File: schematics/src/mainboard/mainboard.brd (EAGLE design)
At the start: 160 x 100 mm, 25 parts, among them IC1 MCP4921P, IC3 TL082P, IC4 TINY24/44/84-PU, Q1 16Mhz, T1 3904

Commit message: Updated Schematics & Firmware
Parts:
- added C12, C5, C6: 10uf, resistor:E2,5-5
- added C13, C14, C16, C17, C18: .1uF, rcl:C050-024X044
- added C15: 47pF, rcl:C050-024X044
- added CV_OFFSET: 20k, pot:S64YW
- added D1, D2: 1N4148, diode:DO35-7
- added D3, D4, D5, D6: 1n4148, diode:DO35-7
- added IC2, IC5, IC7: TL084P, linear:DIL14
- added IC6: 4013N, 40xx:DIL14
- added IO_CON1, IO_CON2: (no value), pinhead:1X04
- added JP1: (no value), pinhead:2X03
- added PWR: (no value), con-ml:ML10
- added PWR_CON: (no value), pinhead:1X03
- added R12, R25: 47k, rcl:0207/7
- added R13: 33k, rcl:0207/7
- added R14: 27k, rcl:0207/7
- added R15, R16, R17, R21, R30, R34: 100k .1%, rcl:0207/7
- added R18, R31: 200k .1%, rcl:0207/7
- added R19, R26: 6.8k, rcl:0207/7
- added R20: 68k, rcl:0207/7
- added R22, R24: 300k, rcl:0207/7
- added R23, R32, R42: 150k, rcl:0207/7
- added R27: 20k 1%, rcl:0207/7
- added R28: 24k 1%, rcl:0207/7
- added R29: 18k, rcl:0207/7
- added R33: 50k .1%, rcl:0207/7
- added R35, R38: 10k, rcl:0207/7
- added R36: 470k, rcl:0207/7
- added R37: 12k, rcl:0207/7
- added R39: 22k, rcl:0207/7
- added R40: 15k, rcl:0207/7
- added R41: 1.2k, rcl:0207/7
- added TP1, TP2: (no value), pinhead:1X01
- added VREF_SET: 100k, pot:S64YW
- added VREF_SET1: 50k, pot:S64YW
- C2: value (none) -> 1.5nF
- IC3: value TL082P -> 7805L; device linear:DIL08 -> linear:TO92
- Q1: value 16Mhz -> 20Mhz
- R1: value 200k -> 200k .1%
- R11: value 100k -> 150k; device pot:S64YW -> rcl:0207/7
- R5: value 100k -> 100k .1%
- R6: value 100k -> 33k .1%
- R7: value (none) -> 10k
- moved R9 238.0 mm to (73.7, 75.6)
- moved R10 237.3 mm to (64.1, 74.3)
- moved R11 226.4 mm to (73.0, 55.9)
- moved R8 196.4 mm to (78.1, 29.8)
- moved R7 181.0 mm to (78.1, 32.4)
- moved R6 174.3 mm to (73.7, 83.2)
- moved R5 166.3 mm to (73.7, 78.1)
- moved C10 164.7 mm to (41.9, 25.4)
- moved C4 160.1 mm to (53.3, 57.8)
- moved C9 158.0 mm to (41.9, 22.9)
- moved C2 152.9 mm to (52.7, 81.3)
- moved R4 149.5 mm to (73.0, 66.0)
- moved C7 149.1 mm to (33.7, 40.0), turned to 180 degrees
- moved R2 148.2 mm to (63.5, 83.2)
- moved C8 146.2 mm to (14.6, 40.0)
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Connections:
- removed net INT_SAW_OUT: C1.2, IC3.1, R2.1
- removed net MOSI: IC1.4
- new net CV_INPUT: IO_CON1.2, R16.2
- new net INT_SAW: C1.2, IC2.1, R2.1, R28.2
- new net MISO: IC1.4, IC4.8, JP1.1
- new net N$14: CV_OFFSET.A, R14.2
- new net N$15: CV_OFFSET.E, R13.1
- new net N$16: CV_OFFSET.S, IC2.10, TP1.1
- new net N$17: IC2.9, R15.2, R16.1
- new net N$18: IC6.2, IC6.5
- new net N$19: IC2.8, R15.1, R17.2
- new net N$20: IC2.13, R17.1, R18.2
- new net N$21: IC5.6, R23.1, R24.2
- new net N$22: IC5.2, R11.1, R22.2
- new net N$23: IC5.3, R12.2, R19.1
- new net N$24: IC5.5, R25.2, R26.1
- new net N$25: IC5.12, R20.2, R29.1
- new net N$26: IC5.13, R27.2, R28.1
- new net N$27: C15.2, IC7.6, R21.2, R31.1, R32.1, R33.1
- new net N$28: D3.C, IC7.2, R30.1, R34.2
- new net N$29: D3.A, D4.C, IC7.1
- new net N$30: D4.A, R30.2, R33.2
- new net N$31: IC7.8, R37.1
- new net N$32: IC7.9, R35.2
- new net N$33: D5.A, D6.C, IC5.10, R39.1, R42.2
- new net N$34: R32.2, VREF_SET1.S
- new net N$35: IC7.13, IC7.14
- new net N$36: IC5.9, R40.1, R41.2
- new net PULSE_OUT: IO_CON2.4, R37.2, R38.2
- new net PWM_SET: IC7.10, IO_CON1.1, R36.2
- new net RST: IC4.4, JP1.5, R7.2
- new net SAW_OUT: IC5.14, IO_CON2.2, R21.1, R27.1, R34.1, R35.1
- new net SINE_OUT: IC5.8, IO_CON2.3, R40.2
- new net SQR_OUT: IC5.1, IO_CON1.4, R22.1
- new net SUB_SQR_OUT: IC5.7, IO_CON1.3, R24.1
- new net TRI_OUT: C15.1, IC7.7, IO_CON2.1, R31.2, R42.1
- net +12V: now also C14.2, C17.2, C5.+, IC2.4, IC3.3, IC5.4, IC7.4, PWR.1, PWR.2, PWR_CON.3, R12.1, R13.2, R20.1, R25.1, VREF_SET1.E; no longer IC3.8
- net +5V: now also C12.+, C18.2, D2.C, IC3.1, IC6.14, JP1.2
- net -12V: now also C13.2, C16.2, C6.-, IC2.11, IC5.11, IC7.11, PWR.10, PWR.9, PWR_CON.1, R14.1; no longer IC3.4
- net CLOCK: now also IC4.7, IC6.3, JP1.4, R11.2; no longer IC4.5
- net DAC_CS: now also IC4.10
- net FRQ_SET: now also D1.C, D2.A, IC2.14, R18.1
- net GND: now also C12.-, C13.1, C14.1, C16.1, C17.1, C18.1, C5.-, C6.+, D1.A, D5.C, D6.A, IC2.12, IC2.3, IC2.5, IC3.2, IC6.10, IC6.4, IC6.6, IC6.7, IC6.8, IC7.12, IC7.3, IC7.5, JP1.6, PWR.3, PWR.4, PWR.5, PWR.6, PWR.7, PWR.8, PWR_CON.2, R19.2, R26.2, R29.2, R36.1, R38.1, R39.2, R41.1, VREF_SET1.A; no longer IC3.3, IC3.5
- net N$1: now also IC2.2; no longer IC3.2
- net N$10: now also IC6.1, R23.2; no longer IC4.4, R7.2
- net N$12: now also VREF_SET.A; no longer R11.A
- net N$13: now also VREF_SET.S; no longer R11.S
- net N$4: now also VREF_SET.E; no longer R11.E
- net N$6: now also IC2.7; no longer IC3.7
- net N$8: now also IC2.6; no longer IC3.6
- net SCK: now also IC4.9, JP1.3
- net VREF: now also TP2.1
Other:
- board size 160 x 100 mm -> 47.9 x 99 mm

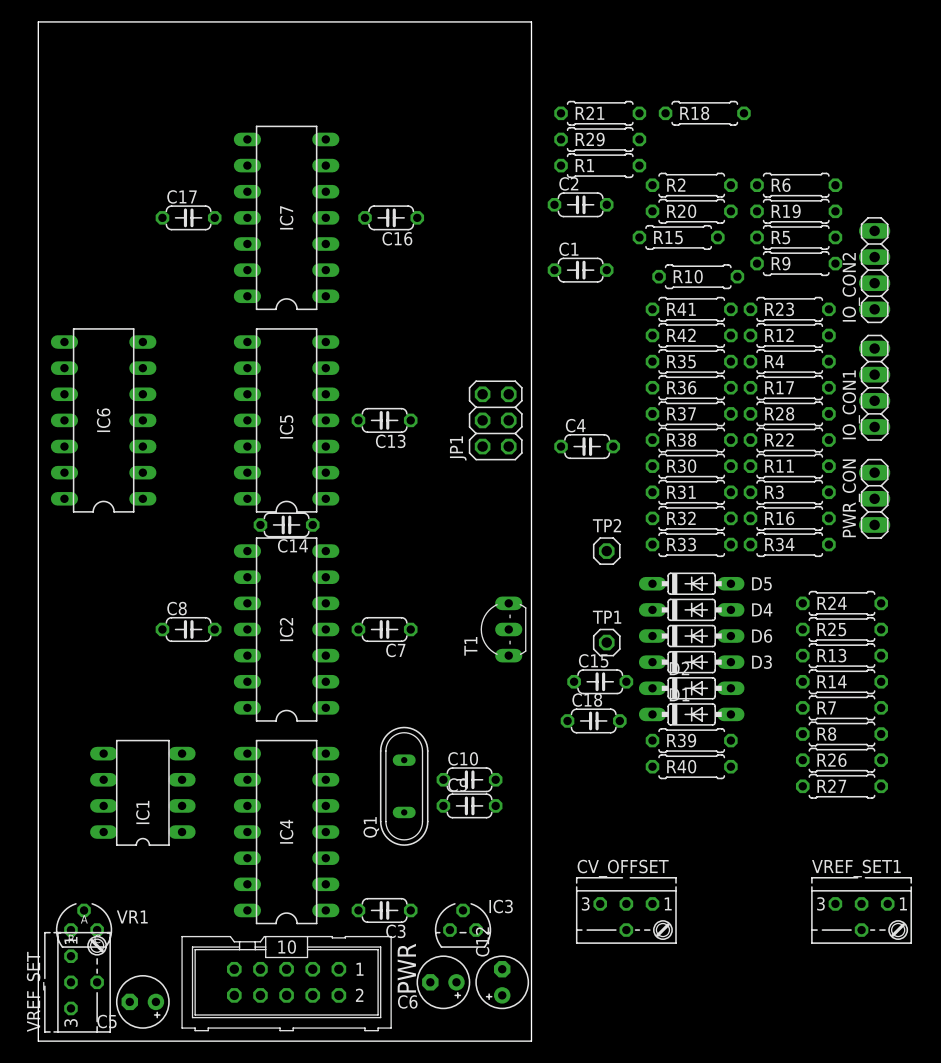
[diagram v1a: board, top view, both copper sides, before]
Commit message: Updated Schematics, Fixed Power Socket orientation
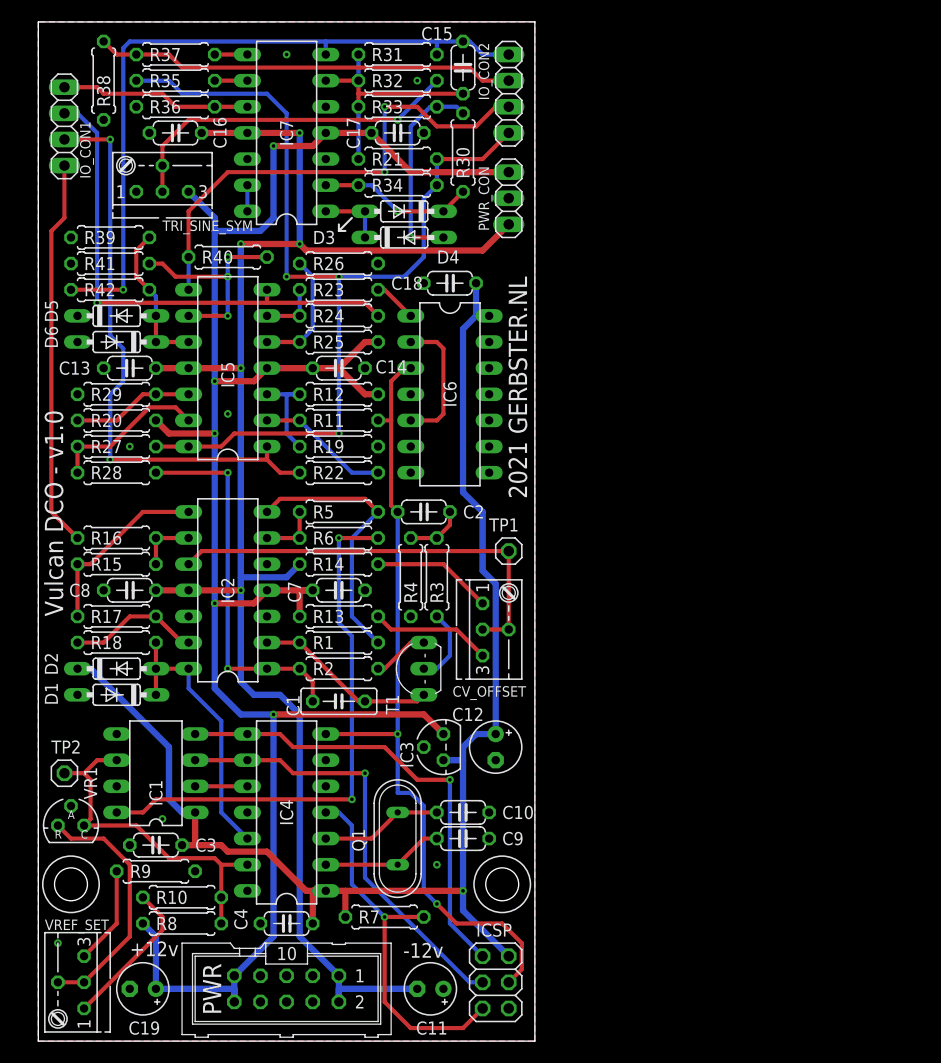
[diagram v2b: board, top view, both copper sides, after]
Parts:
- removed C5, C6: 10uf, resistor:E2,5-5
- removed JP1: (no value), pinhead:2X03
- removed VREF_SET1: 50k, pot:S64YW
- added C11, C19: 10uf, resistor:E2,5-5
- added ICSP: (no value), pinhead:2X03
- added TRI_SINE_SYM: 50k, pot:S64YW
- C1: device rcl:C050-024X044 -> rcl:C050-025X075
- moved R9 85.8 mm to (11.4, 16.5), turned to 180 degrees
- moved IO_CON1 82.7 mm to (2.54, 88.9), turned to 270 degrees
- moved R10 78.5 mm to (14.0, 14.0)
- moved R27 77.8 mm to (7.62, 57.8), turned to 180 degrees
- moved R18 76.9 mm to (7.62, 38.7), turned to 180 degrees
- moved R39 74.7 mm to (6.99, 78.1), turned to 180 degrees
- moved R17 69.1 mm to (7.62, 41.3), turned to 180 degrees
- moved R26 68.7 mm to (29.2, 75.6)
- moved R40 67.0 mm to (18.4, 76.2), turned to 180 degrees
- moved R38 67.0 mm to (6.35, 93.3), turned to 90 degrees
- moved R8 66.7 mm to (14.0, 11.4)
- moved R28 65.7 mm to (7.62, 55.2)
- moved R16 65.4 mm to (7.62, 48.9), turned to 180 degrees
- moved R15 63.2 mm to (7.62, 46.4)
- moved D6 62.8 mm to (7.62, 67.9), turned to 180 degrees
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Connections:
- net +12V: now also C19.+, PWR.10, PWR.9, TRI_SINE_SYM.E; no longer C5.+, PWR.1, PWR.2, VREF_SET1.E
- net +5V: now also ICSP.2; no longer JP1.2
- net -12V: now also C11.-, PWR.1, PWR.2; no longer C6.-, PWR.10, PWR.9
- net CLOCK: now also ICSP.4; no longer JP1.4
- net CV_INPUT: now also IO_CON1.4; no longer IO_CON1.2
- net GND: now also C11.+, C19.-, ICSP.6, TRI_SINE_SYM.A; no longer C5.-, C6.+, JP1.6, VREF_SET1.A
- net MISO: now also ICSP.1; no longer JP1.1
- net N$34: now also TRI_SINE_SYM.S; no longer VREF_SET1.S
- net PULSE_OUT: now also IO_CON2.3; no longer IO_CON2.4
- net RST: now also ICSP.5; no longer JP1.5
- net SAW_OUT: now also IO_CON2.1; no longer IO_CON2.2
- net SCK: now also ICSP.3; no longer JP1.3
- net SINE_OUT: now also IO_CON2.2; no longer IO_CON2.3
- net SQR_OUT: now also IO_CON1.3; no longer IO_CON1.4
- net SUB_SQR_OUT: now also IO_CON1.2; no longer IO_CON1.3
- net TRI_OUT: now also IO_CON2.4; no longer IO_CON2.1
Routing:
- net +12V: track 0.00 -> 199.3 mm, vias 0 -> 5
- net -12V: track 0.00 -> 158.4 mm, vias 0 -> 5
- net +5V: track 0.00 -> 132.9 mm, vias 0 -> 1
- net SAW_OUT: track 0.00 -> 97.6 mm, vias 0 -> 3
- net CLOCK: track 0.00 -> 78.2 mm, vias 0 -> 2
- net TRI_OUT: track 0.00 -> 69.4 mm, vias 0 -> 1
- net SQR_OUT: track 0.00 -> 56.8 mm, vias 0 -> 2
- net N$9: track 0.00 -> 53.1 mm, vias 0 -> 2
- net SUB_SQR_OUT: track 0.00 -> 49.6 mm, vias 0 -> 1
- net SINE_OUT: track 0.00 -> 48.2 mm, vias 0 -> 2
- net MISO: track 0.00 -> 45.1 mm, vias 0 -> 1
- net SCK: track 0.00 -> 42.8 mm, vias 0 -> 1
- net N$16: track 0.00 -> 41.8 mm
- net PULSE_OUT: track 0.00 -> 40.9 mm
- net CV_INPUT: track 0.00 -> 37.8 mm
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- added copper zone on layer 1, net GND
- added copper zone on layer 16, net GND
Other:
- board size 47.9 x 99 mm -> 48.3 x 99.1 mm
- board text added: "+12v"
- board text added: "-12v"
- board text added: "2021 GERBSTER.NL"
- board text added: "Vulcan DCO - v1.0"
